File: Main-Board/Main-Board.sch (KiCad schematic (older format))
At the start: 17 parts, among them J1 Power In, J2 ESC_1, J3 ESC_2, J4 ESC_3, J5 ESC_4, U1 MCP6001U

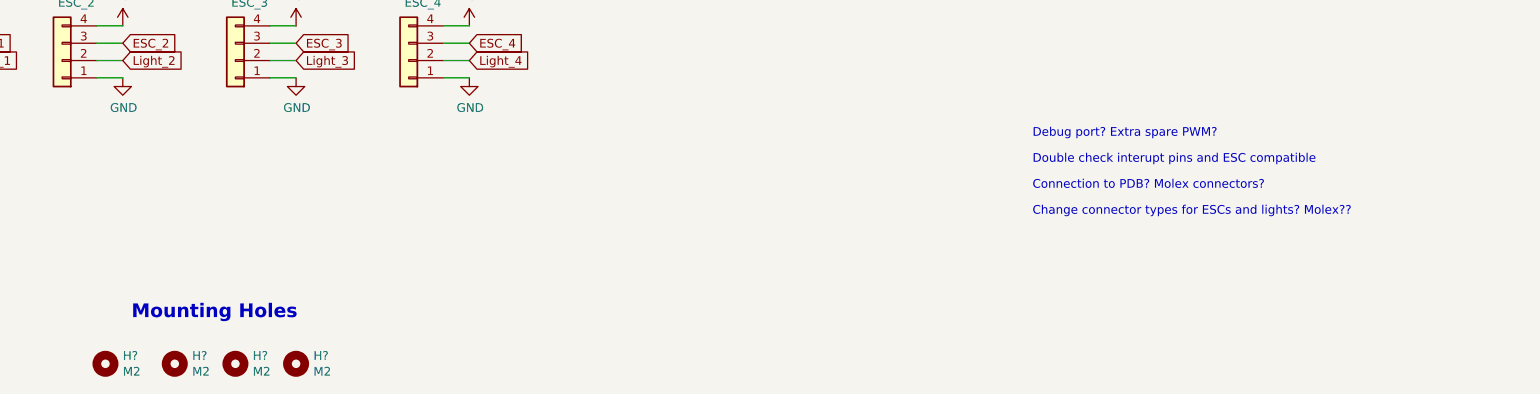
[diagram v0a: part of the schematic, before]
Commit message: Everything is in the schematic. Just need to review board then start the layout. Printed off hard copy
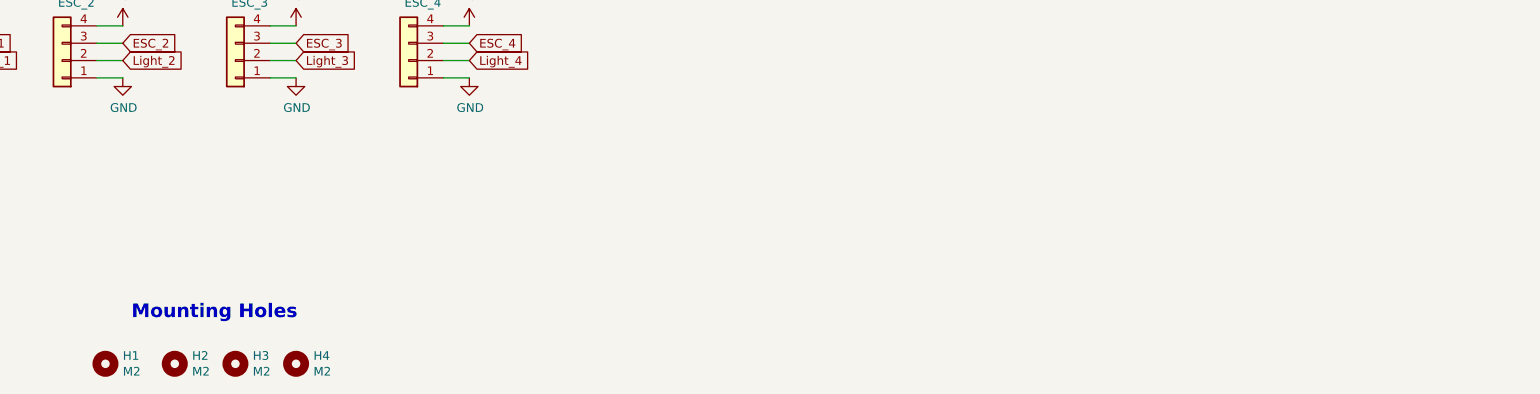
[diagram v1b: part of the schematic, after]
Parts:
- D1: footprint (none) -> Custom:RGB_LED
- gave numbers to parts that had none: 4
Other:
- note removed: "Change connector types for ESCs and lights? Molex??"
- note removed: "Connection to PDB? Molex connectors?"
- note removed: "Debug port? Extra spare PWM?\n"
- note removed: "Double check interupt pins and ESC compatible"
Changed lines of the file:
@@
 F1 "Microcontroller.sch" 50
 $EndSheet
-Text Notes 7800 6250 0    50   ~ 0
-Double check interupt pins and ESC compatible
-Text Notes 7800 6400 0    50   ~ 0
-Connection to PDB? Molex connectors?
-Text Notes 7800 6100 0    50   ~ 0
-Debug port? Extra spare PWM?\n
 $Comp
 L Connector_Generic:Conn_01x02 J1
@@
 	0    1    1    0
 $EndComp
-Text Notes 7800 6550 0    50   ~ 0
-Change connector types for ESCs and lights? Molex??
 Text Notes 2350 750  0    79   ~ 16
 Microcontroller and IMU
@@
 F 0 "D1" H 8350 4947 50  0000 C CNN
 F 1 "LED_RGB" H 8350 4856 50  0000 C CNN
-F 2 "" H 8350 4400 50  0001 C CNN
+F 2 "Custom:RGB_LED" H 8350 4400 50  0001 C CNN
 F 3 "~" H 8350 4400 50  0001 C CNN
 	1    8350 4450
@@
 	4400 5650 4550 5650
 $Comp
-L Mechanical:MountingHole H?
+L Mechanical:MountingHole H1
 U 1 1 5FDEB61F
 P 2450 7400
-F 0 "H?" H 2550 7446 50  0000 L CNN
+F 0 "H1" H 2550 7446 50  0000 L CNN
 F 1 "M2" H 2550 7355 50  0000 L CNN
 F 2 "MountingHole:MountingHole_2.2mm_M2_ISO7380_Pad" H 2450 7400 50  0001 C CNN
@@
 $EndComp
 $Comp
-L Mechanical:MountingHole H?
+L Mechanical:MountingHole H2
 U 1 1 5FDEDAAD
 P 2850 7400
-F 0 "H?" H 2950 7446 50  0000 L CNN
+F 0 "H2" H 2950 7446 50  0000 L CNN
 F 1 "M2" H 2950 7355 50  0000 L CNN
 F 2 "MountingHole:MountingHole_2.2mm_M2_ISO7380_Pad" H 2850 7400 50  0001 C CNN
@@
 $EndComp
 $Comp
-L Mechanical:MountingHole H?
+L Mechanical:MountingHole H3
 U 1 1 5FDEF850
 P 3200 7400
-F 0 "H?" H 3300 7446 50  0000 L CNN
+F 0 "H3" H 3300 7446 50  0000 L CNN
 F 1 "M2" H 3300 7355 50  0000 L CNN
 F 2 "MountingHole:MountingHole_2.2mm_M2_ISO7380_Pad" H 3200 7400 50  0001 C CNN
@@
 $EndComp
 $Comp
-L Mechanical:MountingHole H?
+L Mechanical:MountingHole H4
 U 1 1 5FDF1549
 P 3550 7400
-F 0 "H?" H 3650 7446 50  0000 L CNN
+F 0 "H4" H 3650 7446 50  0000 L CNN
 F 1 "M2" H 3650 7355 50  0000 L CNN
 F 2 "MountingHole:MountingHole_2.2mm_M2_ISO7380_Pad" H 3550 7400 50  0001 C CNN

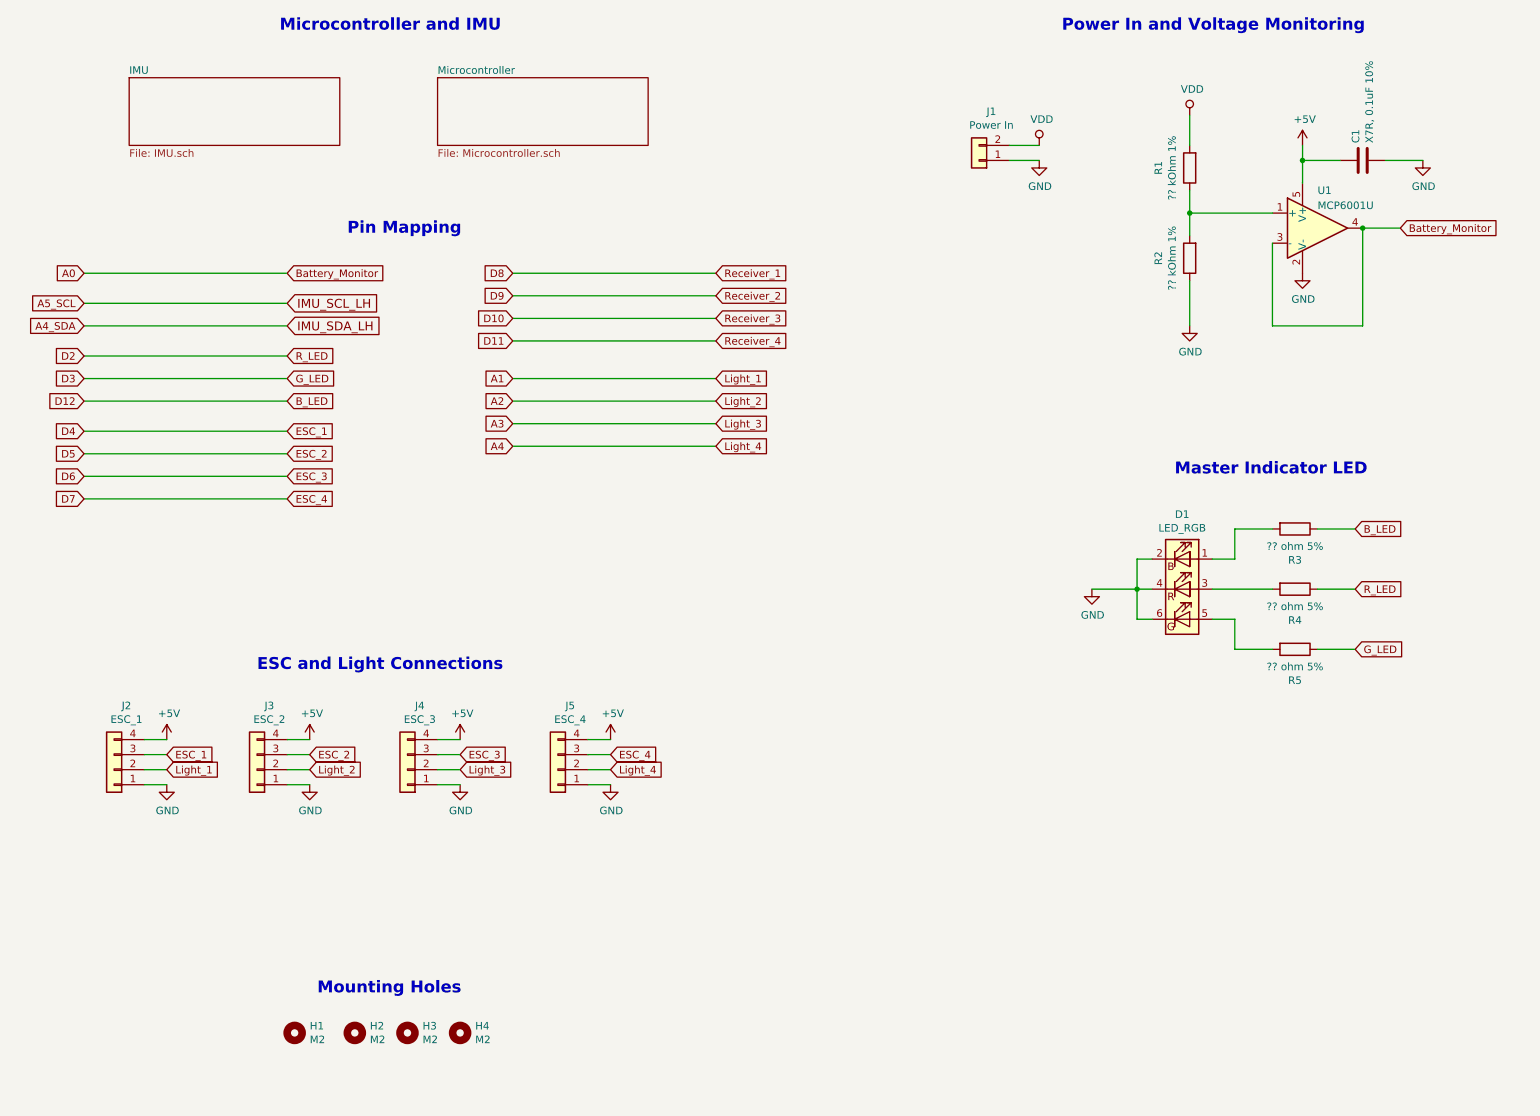
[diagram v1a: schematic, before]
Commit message: Checked over page one, biggest question is what connectors to use
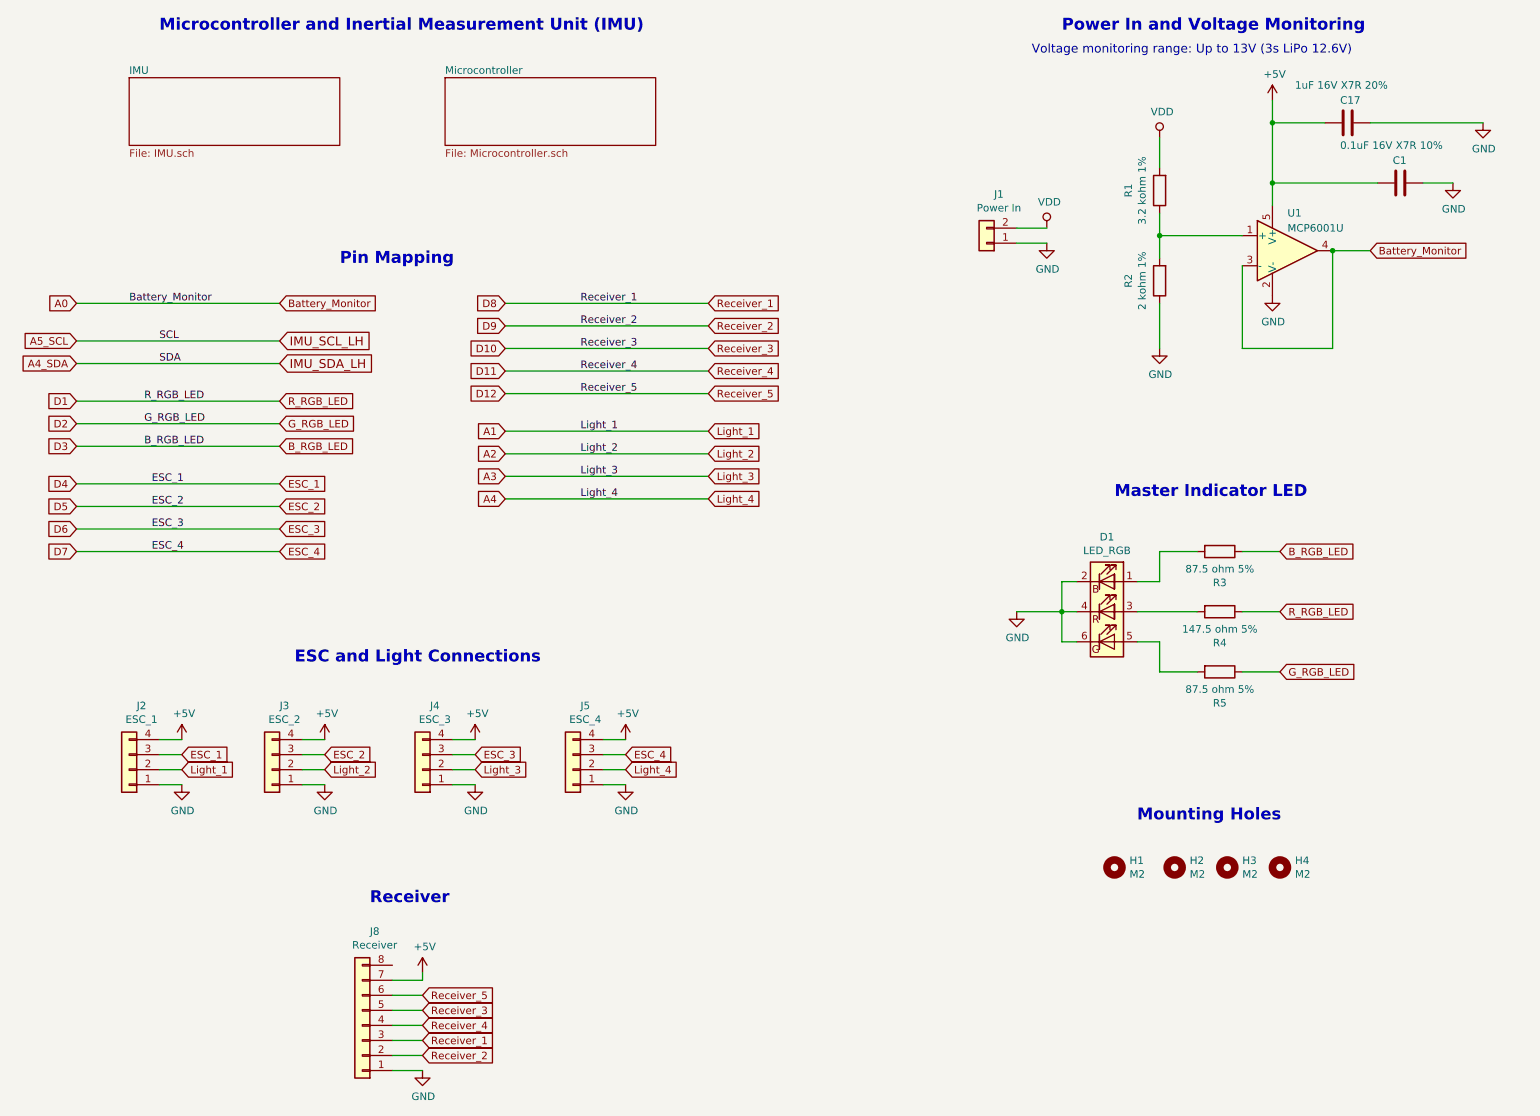
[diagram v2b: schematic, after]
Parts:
- added C17: 1uF 16V X7R 20%, Capacitor_SMD:C_0603_1608Metric_Pad1.05x0.95mm_HandSolder, symbol Device:C
- added J8: Receiver, Connector_Molex:Molex_Micro-Fit_3.0_43045-0800_2x04_P3.00mm_Horizontal, symbol Connector_Generic:Conn_01x08
- C1: value X7R, 0.1uF 10% -> 0.1uF 16V X7R 10%
- D1: Digi-Key # (none) -> 1080-EAST1616RGBA4CT-ND; Digi-Key LinkDigi LinkDigi-Key Link (none) -> https://www.digikey.ca/en/products/detail/everlight-electro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; Manufacturer (none) -> Everlight Electronics Co Ltd; Manufacturer # (none) -> EAST1616RGBA4
- J1: Digi-Key # (none) -> WM1860-ND; Digi-Key LinkDigi LinkDigi-Key Link (none) -> https://www.digikey.ca/en/products/detail/molex/0436500200/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; Manufacturer (none) -> Molex; Manufacturer # (none) -> 0436500200
- J2, J3, J4, J5: footprint Connector_PinHeader_2.54mm:PinHeader_1x04_P2.54mm_Vertical -> Connector_Molex:Molex_Micro-Fit_3.0_43045-0400_2x02_P3.00mm_Horizontal
- R1: value ?? kOhm 1% -> 3.2 kohm 1%
- R2: value ?? kOhm 1% -> 2 kohm 1%
- R3, R5: value ?? ohm 5% -> 87.5 ohm 5%
- R4: value ?? ohm 5% -> 147.5 ohm 5%
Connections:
- net D3 is gone; now on net D2: R5.1
- net +5V: now also C1.2, C17.2, J8.7 (Pin_7); no longer C1.1
- net D10: now also J8.5 (Pin_5)
- net D11: now also J8.4 (Pin_4)
- net D2: no longer R4.1
- net D8: now also J8.3 (Pin_3)
- net D9: now also J8.2 (Pin_2)
- net GND: now also C1.1, C17.1, J8.1 (Pin_1); no longer C1.2
- net B_LED renamed B_RGB_LED
- new net D1: R4.1
- new net D12: J8.6 (Pin_6)
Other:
- note added: "Microcontroller and Inertial Measurement Unit (IMU)"
- note added: "Receiver"
- note added: "Voltage monitoring range: Up to 13V (3s LiPo 12.6V)"
- note removed: "Microcontroller and IMU"
- moved on the sheet: C1, D1, H1, H2, H3, H4, J1, J2, J3, J4, J5, R1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

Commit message: Change to JST-GH connectors
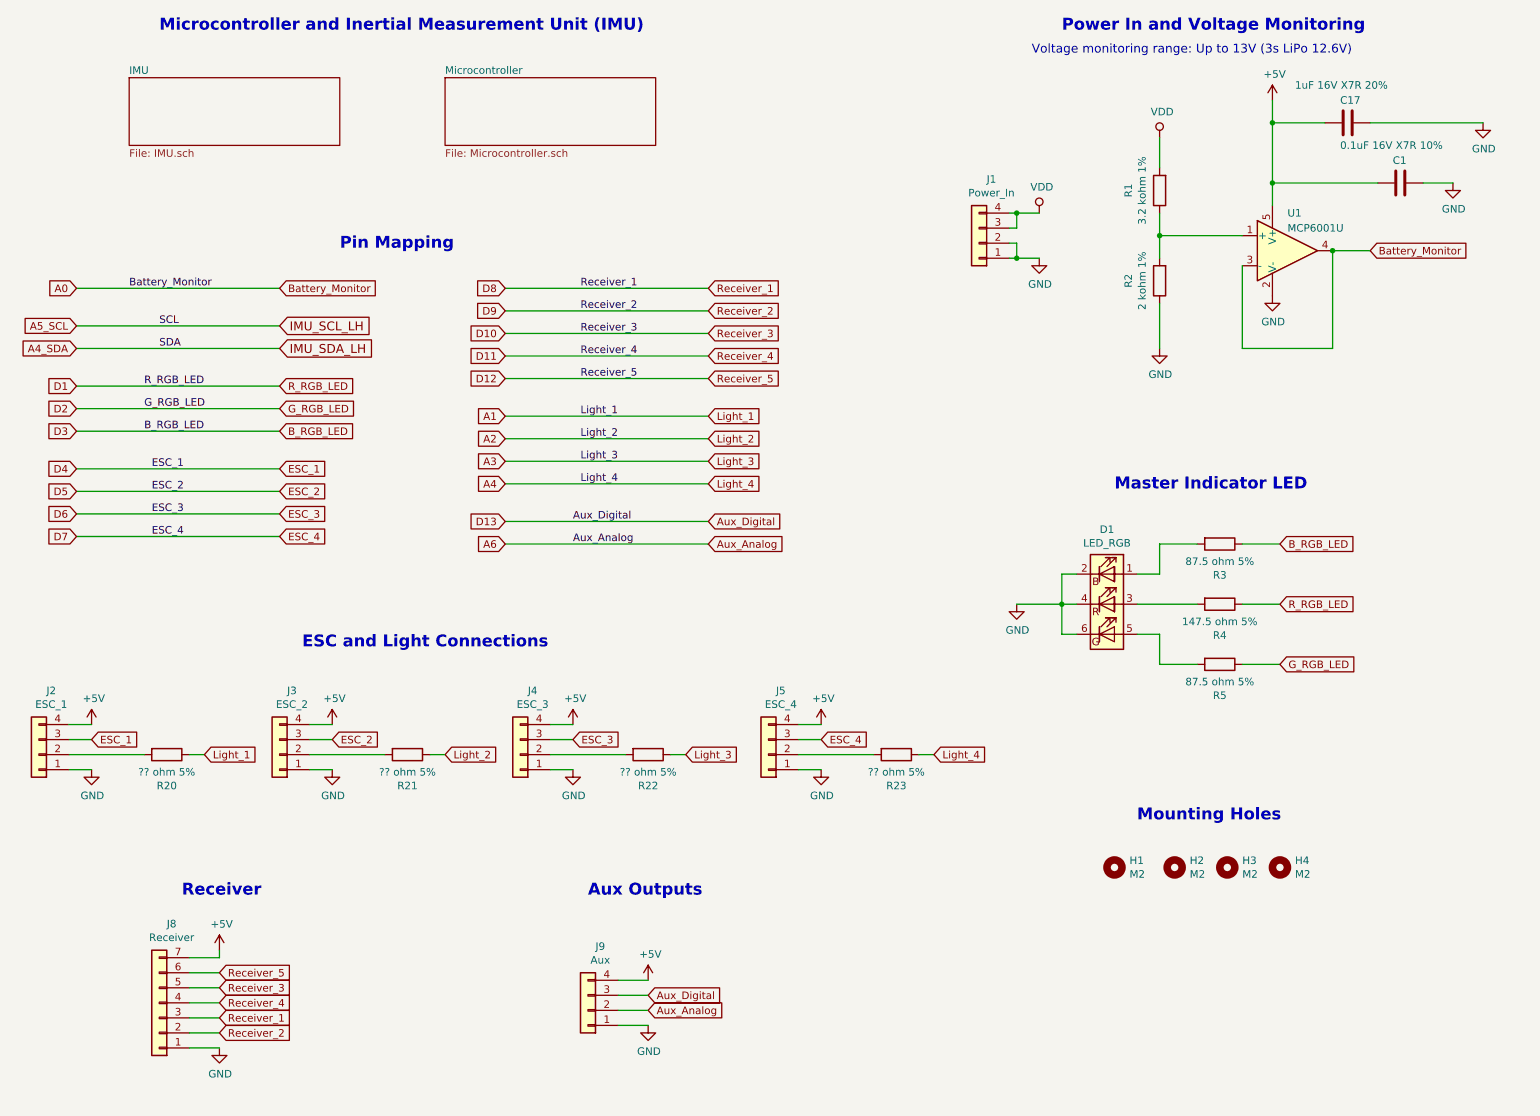
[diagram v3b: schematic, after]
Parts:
- removed J1: Power In, Connector_Molex:Molex_Micro-Fit_3.0_43650-0200_1x02_P3.00mm_Horizontal, symbol Connector_Generic:Conn_01x02
- removed J8: Receiver, Connector_Molex:Molex_Micro-Fit_3.0_43045-0800_2x04_P3.00mm_Horizontal, symbol Connector_Generic:Conn_01x08
- added J1: Power_In, Connector_JST:JST_GH_BM04B-GHS-TBT_1x04-1MP_P1.25mm_Vertical, symbol Connector_Generic:Conn_01x04
- added J8: Receiver, Connector_JST:JST_GH_BM07B-GHS-TBT_1x07-1MP_P1.25mm_Vertical, symbol Connector_Generic:Conn_01x07
- added J9: Aux, Connector_JST:JST_GH_BM04B-GHS-TBT_1x04-1MP_P1.25mm_Vertical, symbol Connector_Generic:Conn_01x04
- added R20, R21, R22, R23: ?? ohm 5%, Resistor_SMD:R_0603_1608Metric_Pad1.05x0.95mm_HandSolder, symbol Device:R
- J2, J3, J4, J5: footprint Connector_Molex:Molex_Micro-Fit_3.0_43045-0400_2x02_P3.00mm_Horizontal -> Connector_JST:JST_GH_BM04B-GHS-TBT_1x04-1MP_P1.25mm_Vertical; Digi-Key # (none) -> 455-1580-1-ND; Digi-Key LinkDigi LinkDigi-Key Link (none) -> https://www.digikey.ca/en/products/detail/jst-sales-america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; Manufacturer (none) -> JST Sales America Inc.; Manufacturer # (none) -> BM04B-GHS-TBT(LF)(SN)(N)
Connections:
- net +5V: now also J8.7 (Pin_7), J9.4 (Pin_4)
- net A1: now also R20.1; no longer J2.2 (Pin_2)
- net A2: now also R21.1; no longer J3.2 (Pin_2)
- net A3: now also R22.1; no longer J4.2 (Pin_2)
- net A4: now also R23.1; no longer J5.2 (Pin_2)
- net D10: now also J8.5 (Pin_5)
- net D11: now also J8.4 (Pin_4)
- net D12: now also J8.6 (Pin_6)
- net D8: now also J8.3 (Pin_3)
- net D9: now also J8.2 (Pin_2)
- net GND: now also J1.1 (Pin_1), J1.2 (Pin_2), J8.1 (Pin_1), J9.1 (Pin_1)
- net VDD: now also J1.3 (Pin_3), J1.4 (Pin_4)
- new net: J2.2 (Pin_2), R20.2
- new net: J3.2 (Pin_2), R21.2
- new net: J4.2 (Pin_2), R22.2
- new net: J5.2 (Pin_2), R23.2
- new net A6: J9.2 (Pin_2)
- new net Aux_Digital: J9.3 (Pin_3)
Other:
- note added: "Aux Outputs"
- moved on the sheet: D1, R3, R4, R5
